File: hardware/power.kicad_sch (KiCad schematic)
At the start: 16 parts, among them U1 TPS7A4901DGNT, U2 LD1085D2M-R

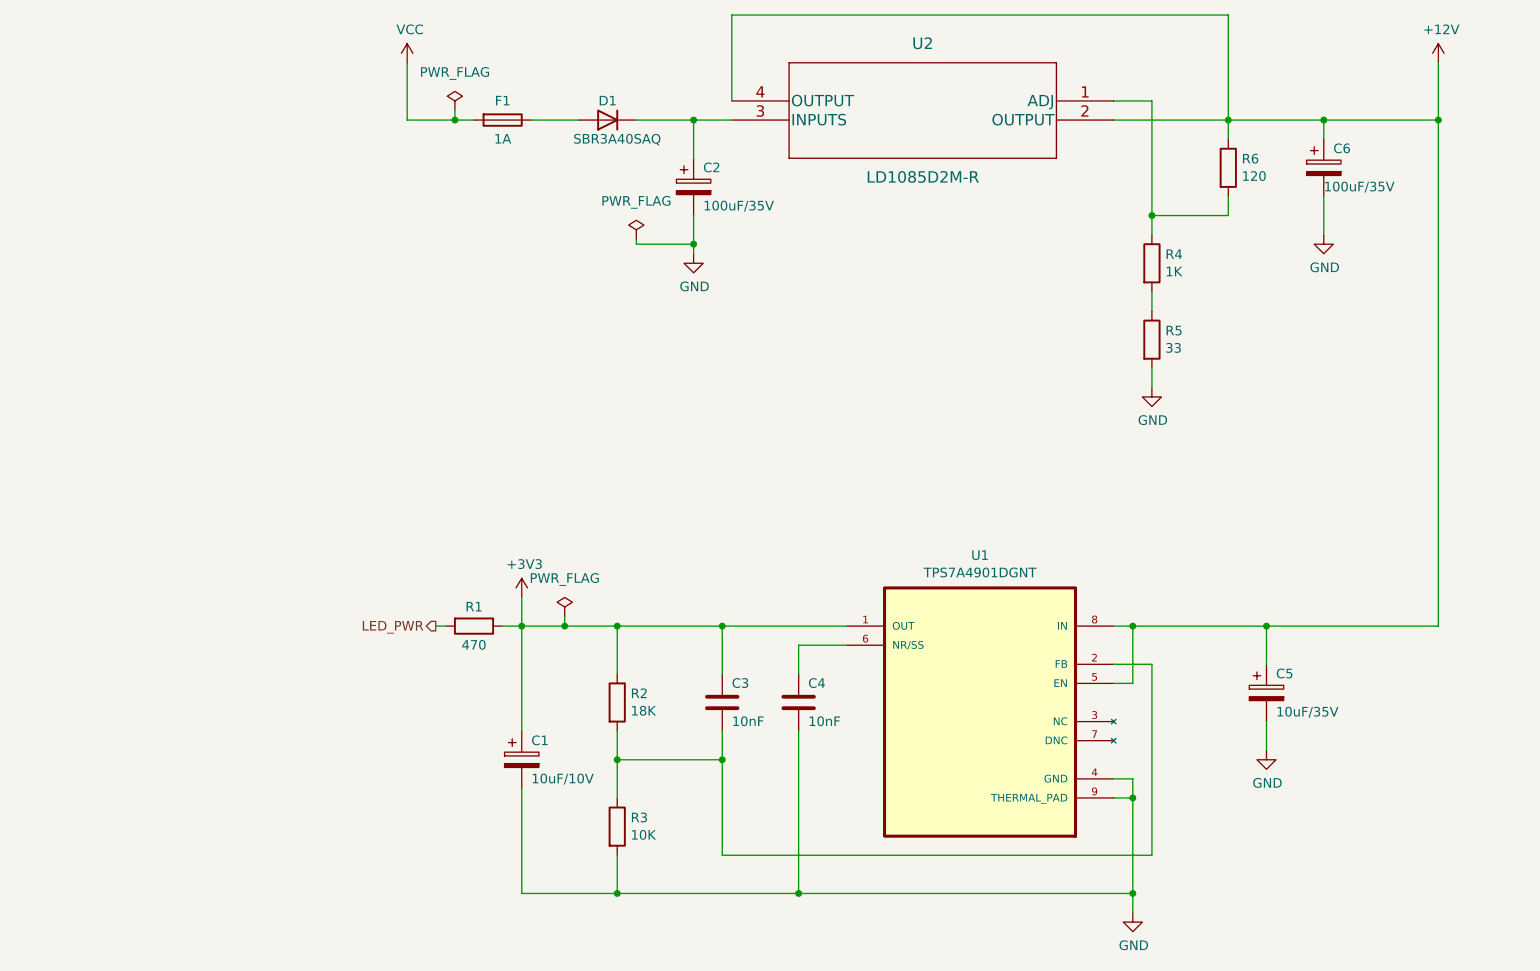
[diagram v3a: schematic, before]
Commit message: Schematics are completed
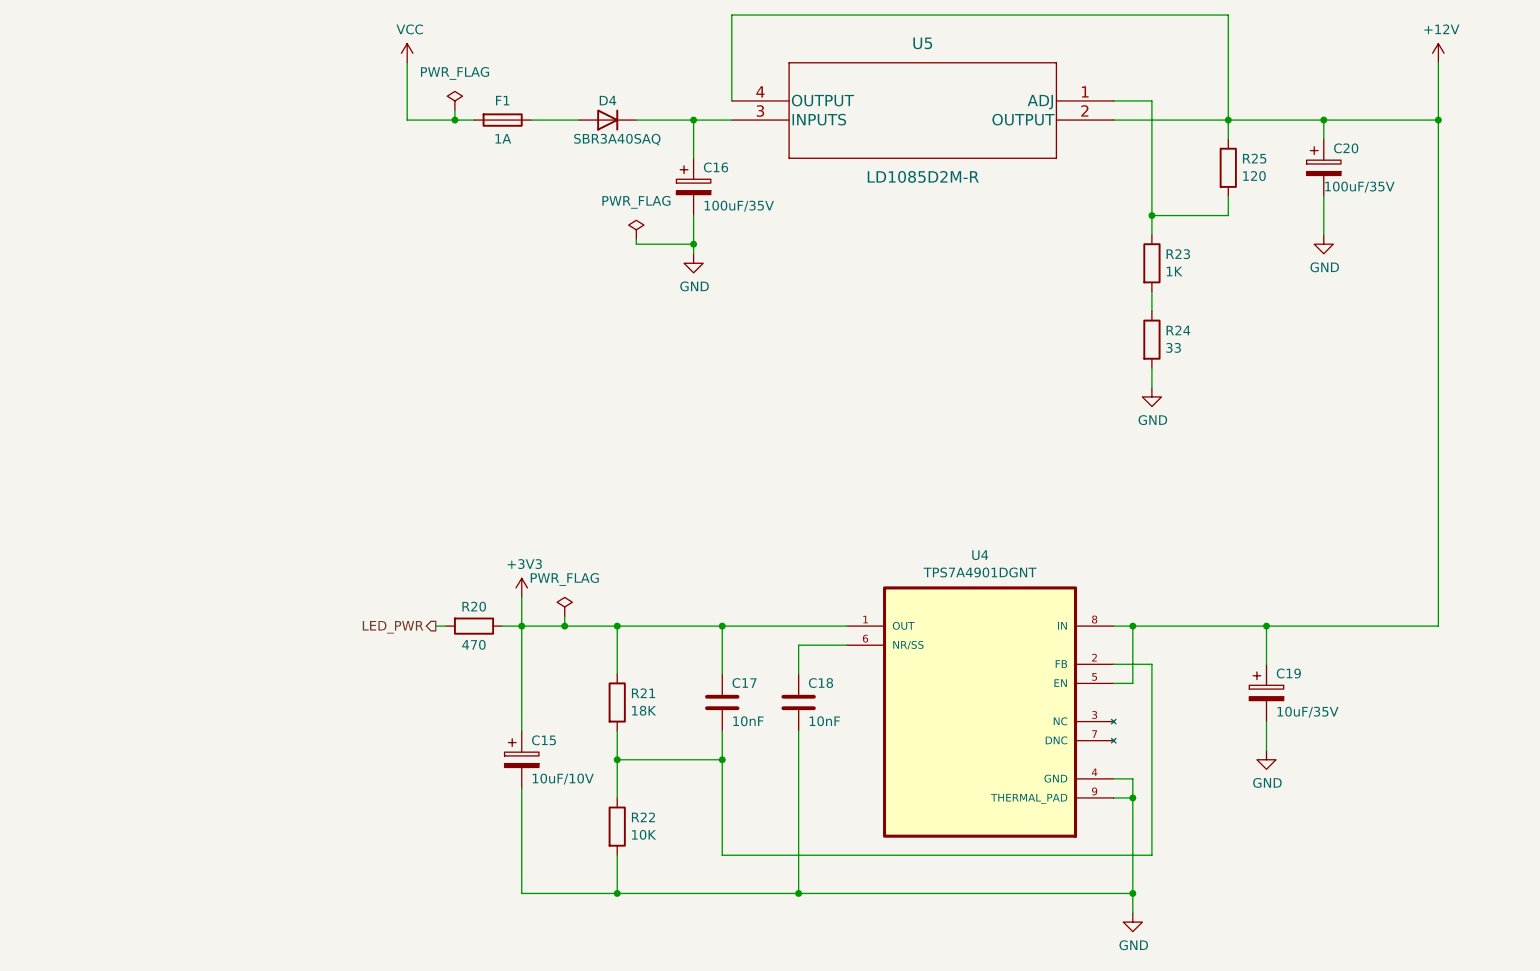
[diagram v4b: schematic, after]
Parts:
- U4: renamed from U1; footprint TPS7A4901DGNT:SOP65P490X110-9N -> Power:SOP65P490X110-9N
- U5: renamed from U2; footprint LD1085D2MR:LD1085D2M-R -> Power:LD1085D2M-R
- renumbered C1 to C15, C2 to C16, C3 to C17, C4 to C18, C5 to C19, C6 to C20, D1 to D4, R1 to R20, R2 to R21, R3 to R22, R4 to R23, R5 to R24, R6 to R25
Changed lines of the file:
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@@
   (symbol (lib_id "Device:CP") (at 127 53.34 0) (unit 1)
     (in_bom yes) (on_board yes)
-    (property "Reference" "C2" (id 0) (at 128.27 50.8 0)
+    (property "Reference" "C16" (id 0) (at 128.27 50.8 0)
       (effects (font (size 1.27 1.27)) (justify left))
     )
@@
   (symbol (lib_id "Device:D") (at 115.57 44.45 180) (unit 1)
     (in_bom yes) (on_board yes)
-    (property "Reference" "D1" (id 0) (at 115.57 41.91 0))
+    (property "Reference" "D4" (id 0) (at 115.57 41.91 0))
     (property "Value" "SBR3A40SAQ" (id 1) (at 116.84 46.99 0))
     (property "Footprint" "Diode_SMD:D_SMB_Handsoldering" (id 2) (at 115.57 44.45 0)
@@
   (symbol (lib_id "Device:R") (at 198.12 50.8 0) (unit 1)
     (in_bom yes) (on_board yes)
-    (property "Reference" "R6" (id 0) (at 199.898 49.6316 0)
+    (property "Reference" "R25" (id 0) (at 199.898 49.6316 0)
       (effects (font (size 1.27 1.27)) (justify left))
     )
@@
   (symbol (lib_id "Device:R") (at 187.96 63.5 0) (unit 1)
     (in_bom yes) (on_board yes)
-    (property "Reference" "R4" (id 0) (at 189.738 62.3316 0)
+    (property "Reference" "R23" (id 0) (at 189.738 62.3316 0)
       (effects (font (size 1.27 1.27)) (justify left))
     )
@@
   (symbol (lib_id "Device:CP") (at 210.82 50.8 0) (unit 1)
     (in_bom yes) (on_board yes)
-    (property "Reference" "C6" (id 0) (at 212.09 48.26 0)
+    (property "Reference" "C20" (id 0) (at 212.09 48.26 0)
       (effects (font (size 1.27 1.27)) (justify left))
     )
@@
   (symbol (lib_id "power:GND") (at 187.96 80.01 0) (unit 1)
     (in_bom yes) (on_board yes)
-    (property "Reference" "#PWR015" (id 0) (at 187.96 86.36 0)
+    (property "Reference" "#PWR034" (id 0) (at 187.96 86.36 0)
       (effects (font (size 1.27 1.27)) hide)
     )
@@
   (symbol (lib_id "TPS7A4901DGNT:TPS7A4901DGNT") (at 165.1 119.38 0) (mirror y) (unit 1)
     (in_bom yes) (on_board yes)
-    (property "Reference" "U1" (id 0) (at 165.1 102.362 0))
+    (property "Reference" "U4" (id 0) (at 165.1 102.362 0))
     (property "Value" "TPS7A4901DGNT" (id 1) (at 165.1 104.6734 0))
-    (property "Footprint" "TPS7A4901DGNT:SOP65P490X110-9N" (id 2) (at 165.1 119.38 0)
+    (property "Footprint" "Power:SOP65P490X110-9N" (id 2) (at 165.1 119.38 0)
       (effects (font (size 1.27 1.27)) (justify left bottom) hide)
     )
@@
   (symbol (lib_id "Device:C") (at 140.97 121.92 0) (unit 1)
     (in_bom yes) (on_board yes)
-    (property "Reference" "C4" (id 0) (at 142.24 119.38 0)
+    (property "Reference" "C18" (id 0) (at 142.24 119.38 0)
       (effects (font (size 1.27 1.27)) (justify left))
     )
@@
   (symbol (lib_id "Device:CP") (at 203.2 120.65 0) (unit 1)
     (in_bom yes) (on_board yes)
-    (property "Reference" "C5" (id 0) (at 204.47 118.11 0)
+    (property "Reference" "C19" (id 0) (at 204.47 118.11 0)
       (effects (font (size 1.27 1.27)) (justify left))
     )
@@
   (symbol (lib_id "power:GND") (at 203.2 128.27 0) (unit 1)
     (in_bom yes) (on_board yes)
-    (property "Reference" "#PWR016" (id 0) (at 203.2 134.62 0)
+    (property "Reference" "#PWR035" (id 0) (at 203.2 134.62 0)
       (effects (font (size 1.27 1.27)) hide)
     )
@@
   (symbol (lib_id "power:GND") (at 185.42 149.86 0) (unit 1)
     (in_bom yes) (on_board yes)
-    (property "Reference" "#PWR014" (id 0) (at 185.42 156.21 0)
+    (property "Reference" "#PWR033" (id 0) (at 185.42 156.21 0)
       (effects (font (size 1.27 1.27)) hide)
     )
@@
   (symbol (lib_id "power:+3V3") (at 104.14 107.95 0) (unit 1)
     (in_bom yes) (on_board yes)
-    (property "Reference" "#PWR012" (id 0) (at 104.14 111.76 0)
+    (property "Reference" "#PWR031" (id 0) (at 104.14 111.76 0)
       (effects (font (size 1.27 1.27)) hide)
     )
@@
   (symbol (lib_id "Device:C") (at 130.81 121.92 0) (unit 1)
     (in_bom yes) (on_board yes)
-    (property "Reference" "C3" (id 0) (at 132.08 119.38 0)
+    (property "Reference" "C17" (id 0) (at 132.08 119.38 0)
       (effects (font (size 1.27 1.27)) (justify left))
     )
@@
   (symbol (lib_id "Device:R") (at 116.84 121.92 0) (unit 1)
     (in_bom yes) (on_board yes)
-    (property "Reference" "R2" (id 0) (at 118.618 120.7516 0)
+    (property "Reference" "R21" (id 0) (at 118.618 120.7516 0)
       (effects (font (size 1.27 1.27)) (justify left))
     )
@@
   (symbol (lib_id "Device:R") (at 116.84 138.43 0) (unit 1)
     (in_bom yes) (on_board yes)
-    (property "Reference" "R3" (id 0) (at 118.618 137.2616 0)
+    (property "Reference" "R22" (id 0) (at 118.618 137.2616 0)
       (effects (font (size 1.27 1.27)) (justify left))
     )
@@
   (symbol (lib_id "Device:CP") (at 104.14 129.54 0) (unit 1)
     (in_bom yes) (on_board yes)
-    (property "Reference" "C1" (id 0) (at 105.41 127 0)
+    (property "Reference" "C15" (id 0) (at 105.41 127 0)
       (effects (font (size 1.27 1.27)) (justify left))
     )
@@
   (symbol (lib_id "power:GND") (at 127 62.23 0) (unit 1)
     (in_bom yes) (on_board yes)
-    (property "Reference" "#PWR013" (id 0) (at 127 68.58 0)
+    (property "Reference" "#PWR032" (id 0) (at 127 68.58 0)
       (effects (font (size 1.27 1.27)) hide)
     )
@@
   (symbol (lib_id "power:+12V") (at 226.06 36.83 0) (unit 1)
     (in_bom yes) (on_board yes)
-    (property "Reference" "#PWR018" (id 0) (at 226.06 40.64 0)
+    (property "Reference" "#PWR037" (id 0) (at 226.06 40.64 0)
       (effects (font (size 1.27 1.27)) hide)
     )
@@
   (symbol (lib_id "power:VCC") (at 88.9 36.83 0) (unit 1)
     (in_bom yes) (on_board yes)
-    (property "Reference" "#PWR011" (id 0) (at 88.9 40.64 0)
+    (property "Reference" "#PWR030" (id 0) (at 88.9 40.64 0)
       (effects (font (size 1.27 1.27)) hide)
     )
@@
   (symbol (lib_id "LD1085D2MR:LD1085D2M-R") (at 182.88 41.91 0) (mirror y) (unit 1)
     (in_bom yes) (on_board yes)
-    (property "Reference" "U2" (id 0) (at 157.48 34.29 0)
+    (property "Reference" "U5" (id 0) (at 157.48 34.29 0)
       (effects (font (size 1.524 1.524)))
     )
@@
       (effects (font (size 1.524 1.524)))
     )
-    (property "Footprint" "LD1085D2MR:LD1085D2M-R" (id 2) (at 157.48 35.814 0)
+    (property "Footprint" "Power:LD1085D2M-R" (id 2) (at 157.48 35.814 0)
       (effects (font (size 1.524 1.524)) hide)
     )
@@
   (symbol (lib_id "power:GND") (at 210.82 59.69 0) (unit 1)
     (in_bom yes) (on_board yes)
-    (property "Reference" "#PWR017" (id 0) (at 210.82 66.04 0)
+    (property "Reference" "#PWR036" (id 0) (at 210.82 66.04 0)
       (effects (font (size 1.27 1.27)) hide)
     )
@@
   (symbol (lib_id "Device:R") (at 187.96 73.66 0) (unit 1)
     (in_bom yes) (on_board yes)
-    (property "Reference" "R5" (id 0) (at 189.738 72.4916 0)
+    (property "Reference" "R24" (id 0) (at 189.738 72.4916 0)
       (effects (font (size 1.27 1.27)) (justify left))
     )
@@
   (symbol (lib_id "Device:R") (at 97.79 111.76 270) (unit 1)
     (in_bom yes) (on_board yes)
-    (property "Reference" "R1" (id 0) (at 97.79 109.22 90))
+    (property "Reference" "R20" (id 0) (at 97.79 109.22 90))
     (property "Value" "470" (id 1) (at 97.79 114.3 90))
     (property "Footprint" "Resistor_SMD:R_0603_1608Metric" (id 2) (at 97.79 109.982 90)
@@
   (symbol (lib_id "power:PWR_FLAG") (at 109.855 110.49 0) (unit 1)
     (in_bom yes) (on_board yes) (fields_autoplaced)
-    (property "Reference" "#FLG02" (id 0) (at 109.855 108.585 0)
+    (property "Reference" "#FLG03" (id 0) (at 109.855 108.585 0)
       (effects (font (size 1.27 1.27)) hide)
     )
@@
   (symbol (lib_id "power:PWR_FLAG") (at 119.38 60.325 0) (unit 1)
     (in_bom yes) (on_board yes) (fields_autoplaced)
-    (property "Reference" "#FLG03" (id 0) (at 119.38 58.42 0)
+    (property "Reference" "#FLG04" (id 0) (at 119.38 58.42 0)
       (effects (font (size 1.27 1.27)) hide)
     )
@@
   (symbol (lib_id "power:PWR_FLAG") (at 95.25 43.18 0) (unit 1)
     (in_bom yes) (on_board yes) (fields_autoplaced)
-    (property "Reference" "#FLG01" (id 0) (at 95.25 41.275 0)
-      (effects (font (size 1.27 1.27)) hide)
-    )
+    (property "Reference" "#FLG02" (id 0) (at 95.25 41.275 0)
+      (effects (font (size 1.27 1.27)) hide)
+    )

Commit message: PCB designed
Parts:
- added J6: PWR INPUT, Connector_Phoenix_MC:PhoenixContact_MC_1,5_2-G-3.81_1x02_P3.81mm_Horizontal, symbol Connector:Screw_Terminal_01x02
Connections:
- net GND: now also J6.1 (Pin_1)
- net VCC: now also J6.2 (Pin_2)
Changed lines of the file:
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@@
+    (stroke (width 0) (type default) (color 0 0 0 0))
+  )
+  (wire (pts (xy 70.358 54.102) (xy 72.4916 54.102))
     (stroke (width 0) (type default) (color 0 0 0 0))
   )
@@
     (stroke (width 0) (type default) (color 0 0 0 0))
   )
+  (wire (pts (xy 70.358 56.642) (xy 71.7296 56.642))
+    (stroke (width 0) (type default) (color 0 0 0 0))
+  )
   (wire (pts (xy 226.06 111.76) (xy 203.2 111.76))
     (stroke (width 0) (type default) (color 0 0 0 0))
@@
   )
   (wire (pts (xy 198.12 54.61) (xy 198.12 57.15))
+    (stroke (width 0) (type default) (color 0 0 0 0))
+  )
+  (wire (pts (xy 71.7296 58.42) (xy 71.7296 56.642))
     (stroke (width 0) (type default) (color 0 0 0 0))
   )
@@
     (pin "1")
   )
+  (symbol (lib_id "power:GND") (at 71.7296 58.42 0) (unit 1)
+    (in_bom yes) (on_board yes)
+    (property "Reference" "#PWR042" (id 0) (at 71.7296 64.77 0)
+      (effects (font (size 1.27 1.27)) hide)
+    )
+    (property "Value" "GND" (id 1) (at 71.8566 62.8142 0))
+    (property "Footprint" "" (id 2) (at 71.7296 58.42 0)
+      (effects (font (size 1.27 1.27)) hide)
+    )
+    (property "Datasheet" "" (id 3) (at 71.7296 58.42 0)
+      (effects (font (size 1.27 1.27)) hide)
+    )
+    (pin "1")
+  )
+  (symbol (lib_id "power:VCC") (at 72.4916 54.102 0) (unit 1)
+    (in_bom yes) (on_board yes)
+    (property "Reference" "#PWR043" (id 0) (at 72.4916 57.912 0)
+      (effects (font (size 1.27 1.27)) hide)
+    )
+    (property "Value" "VCC" (id 1) (at 72.8726 49.7078 0))
+    (property "Footprint" "" (id 2) (at 72.4916 54.102 0)
+      (effects (font (size 1.27 1.27)) hide)
+    )
+    (property "Datasheet" "" (id 3) (at 72.4916 54.102 0)
+      (effects (font (size 1.27 1.27)) hide)
+    )
+    (pin "1")
+  )
   (symbol (lib_id "power:PWR_FLAG") (at 95.25 43.18 0) (unit 1)
     (in_bom yes) (on_board yes) (fields_autoplaced)
@@
     (pin "1")
   )
+  (symbol (lib_id "Connector:Screw_Terminal_01x02") (at 65.278 56.642 180) (unit 1)
+    (in_bom yes) (on_board yes)
+    (property "Reference" "J6" (id 0) (at 59.2836 55.118 90))
+    (property "Value" "PWR INPUT" (id 1) (at 61.8236 55.118 90))
+    (property "Footprint" "Connector_Phoenix_MC:PhoenixContact_MC_1,5_2-G-3.81_1x02_P3.81mm_Horizontal" (id 2) (at 65.278 56.642 0)
+      (effects (font (size 1.27 1.27)) hide)
+    )
+    (property "Datasheet" "~" (id 3) (at 65.278 56.642 0)
+      (effects (font (size 1.27 1.27)) hide)
+    )
+    (pin "1")
+    (pin "2")
+  )
 )

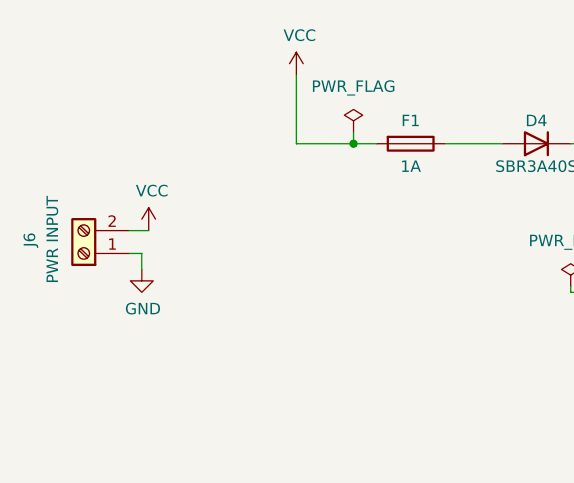
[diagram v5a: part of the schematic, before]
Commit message: Footprints are assigned and Cut edges fixed
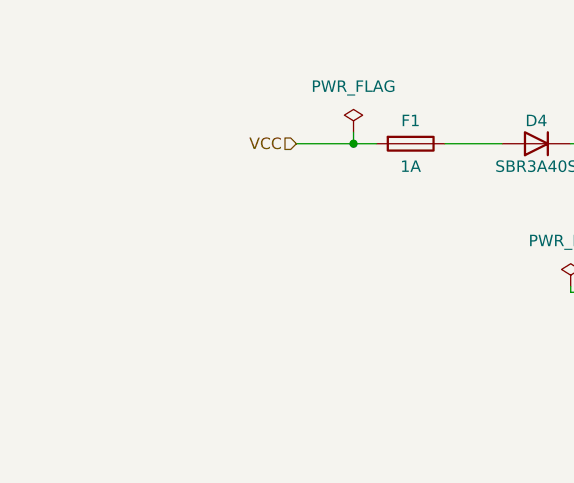
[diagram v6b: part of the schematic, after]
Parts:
- removed J6: PWR INPUT, Connector_Phoenix_MC:PhoenixContact_MC_1,5_2-G-3.81_1x02_P3.81mm_Horizontal, symbol Connector:Screw_Terminal_01x02
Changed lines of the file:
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@@
-    (stroke (width 0) (type default) (color 0 0 0 0))
-  )
-  (wire (pts (xy 70.358 54.102) (xy 72.4916 54.102))
     (stroke (width 0) (type default) (color 0 0 0 0))
   )
@@
     (stroke (width 0) (type default) (color 0 0 0 0))
   )
-  (wire (pts (xy 70.358 56.642) (xy 71.7296 56.642))
-    (stroke (width 0) (type default) (color 0 0 0 0))
-  )
   (wire (pts (xy 226.06 111.76) (xy 203.2 111.76))
     (stroke (width 0) (type default) (color 0 0 0 0))
   )
-  (wire (pts (xy 88.9 36.83) (xy 88.9 44.45))
-    (stroke (width 0) (type default) (color 0 0 0 0))
-  )
   (wire (pts (xy 182.88 116.84) (xy 187.96 116.84))
     (stroke (width 0) (type default) (color 0 0 0 0))
@@
     (stroke (width 0) (type default) (color 0 0 0 0))
   )
-  (wire (pts (xy 71.7296 58.42) (xy 71.7296 56.642))
-    (stroke (width 0) (type default) (color 0 0 0 0))
-  )
   (wire (pts (xy 104.14 125.73) (xy 104.14 111.76))
     (stroke (width 0) (type default) (color 0 0 0 0))
@@
   (wire (pts (xy 210.82 46.99) (xy 210.82 44.45))
     (stroke (width 0) (type default) (color 0 0 0 0))
+  )
+  (hierarchical_label "VCC" (shape input) (at 88.9 44.45 180)
+    (effects (font (size 1.27 1.27)) (justify right))
   )
   (hierarchical_label "LED_PWR" (shape output) (at 92.71 111.76 180)
@@
     (pin "1")
   )
-  (symbol (lib_id "power:VCC") (at 88.9 36.83 0) (unit 1)
-    (in_bom yes) (on_board yes)
-    (property "Reference" "#PWR030" (id 0) (at 88.9 40.64 0)
-      (effects (font (size 1.27 1.27)) hide)
-    )
-    (property "Value" "VCC" (id 1) (at 89.281 32.4358 0))
-    (property "Footprint" "" (id 2) (at 88.9 36.83 0)
-      (effects (font (size 1.27 1.27)) hide)
-    )
-    (property "Datasheet" "" (id 3) (at 88.9 36.83 0)
-      (effects (font (size 1.27 1.27)) hide)
-    )
-    (pin "1")
-  )
   (symbol (lib_id "LD1085D2MR:LD1085D2M-R") (at 182.88 41.91 0) (mirror y) (unit 1)
     (in_bom yes) (on_board yes)
@@
     (pin "1")
   )
-  (symbol (lib_id "power:GND") (at 71.7296 58.42 0) (unit 1)
-    (in_bom yes) (on_board yes)
-    (property "Reference" "#PWR042" (id 0) (at 71.7296 64.77 0)
-      (effects (font (size 1.27 1.27)) hide)
-    )
-    (property "Value" "GND" (id 1) (at 71.8566 62.8142 0))
-    (property "Footprint" "" (id 2) (at 71.7296 58.42 0)
-      (effects (font (size 1.27 1.27)) hide)
-    )
-    (property "Datasheet" "" (id 3) (at 71.7296 58.42 0)
-      (effects (font (size 1.27 1.27)) hide)
-    )
-    (pin "1")
-  )
-  (symbol (lib_id "power:VCC") (at 72.4916 54.102 0) (unit 1)
-    (in_bom yes) (on_board yes)
-    (property "Reference" "#PWR043" (id 0) (at 72.4916 57.912 0)
-      (effects (font (size 1.27 1.27)) hide)
-    )
-    (property "Value" "VCC" (id 1) (at 72.8726 49.7078 0))
-    (property "Footprint" "" (id 2) (at 72.4916 54.102 0)
-      (effects (font (size 1.27 1.27)) hide)
-    )
-    (property "Datasheet" "" (id 3) (at 72.4916 54.102 0)
-      (effects (font (size 1.27 1.27)) hide)
-    )
-    (pin "1")
-  )
   (symbol (lib_id "power:PWR_FLAG") (at 95.25 43.18 0) (unit 1)
     (in_bom yes) (on_board yes) (fields_autoplaced)
@@
     (pin "1")
   )
-  (symbol (lib_id "Connector:Screw_Terminal_01x02") (at 65.278 56.642 180) (unit 1)
-    (in_bom yes) (on_board yes)
-    (property "Reference" "J6" (id 0) (at 59.2836 55.118 90))
-    (property "Value" "PWR INPUT" (id 1) (at 61.8236 55.118 90))
-    (property "Footprint" "Connector_Phoenix_MC:PhoenixContact_MC_1,5_2-G-3.81_1x02_P3.81mm_Horizontal" (id 2) (at 65.278 56.642 0)
-      (effects (font (size 1.27 1.27)) hide)
-    )
-    (property "Datasheet" "~" (id 3) (at 65.278 56.642 0)
-      (effects (font (size 1.27 1.27)) hide)
-    )
-    (pin "1")
-    (pin "2")
-  )
 )
